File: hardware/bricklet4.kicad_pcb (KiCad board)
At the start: 4 copper layers, 102 x 85 mm, 102 parts, among them J101 TNG-Power-TOP, J102 TNG-Power-BTM, J103 TNG-Data-TOP, J104 TNG-Data-BTM, P102 Debug, P103 PE, P201 CON-SENSOR2, P202 CON-SENSOR2, P203 CON-SENSOR2, P204 CON-SENSOR2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

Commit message: fix slew rate bug, mark C as DNP
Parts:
- C206: value 1uF -> DNP

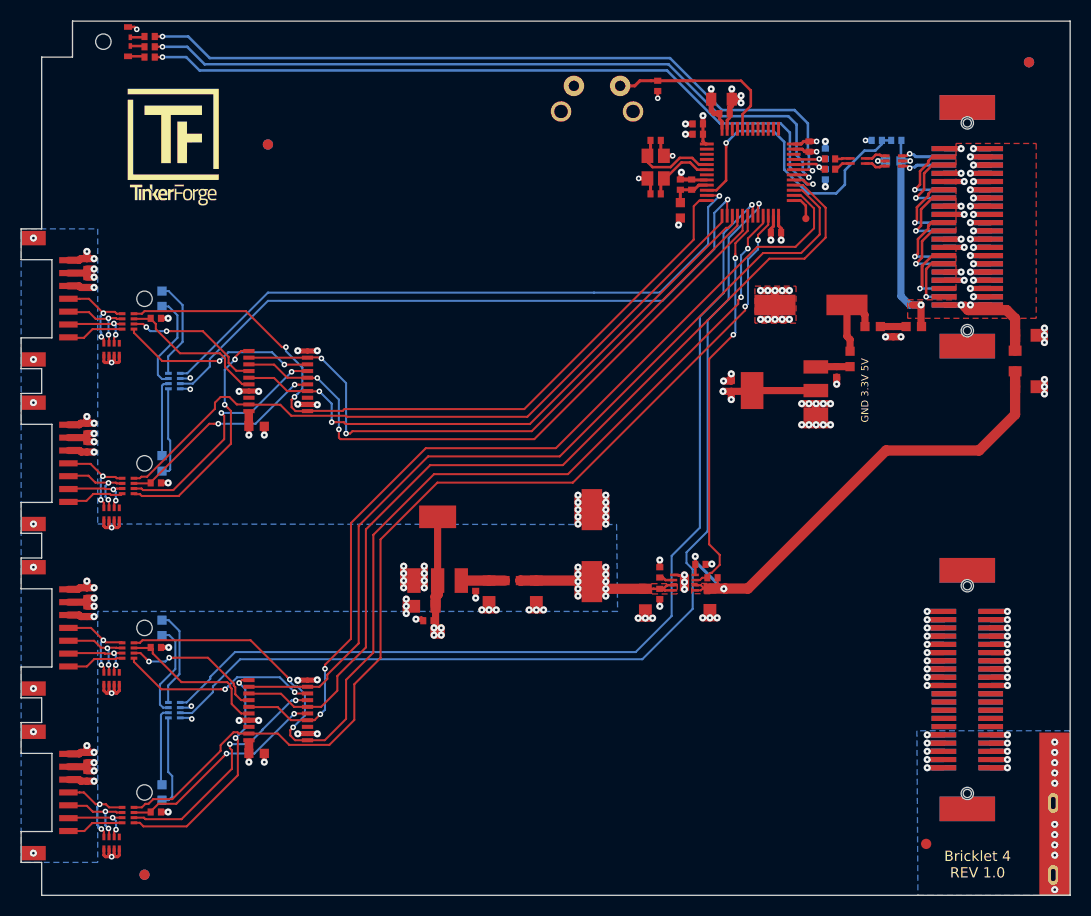
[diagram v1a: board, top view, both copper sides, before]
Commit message: version 1.1
fix footprints
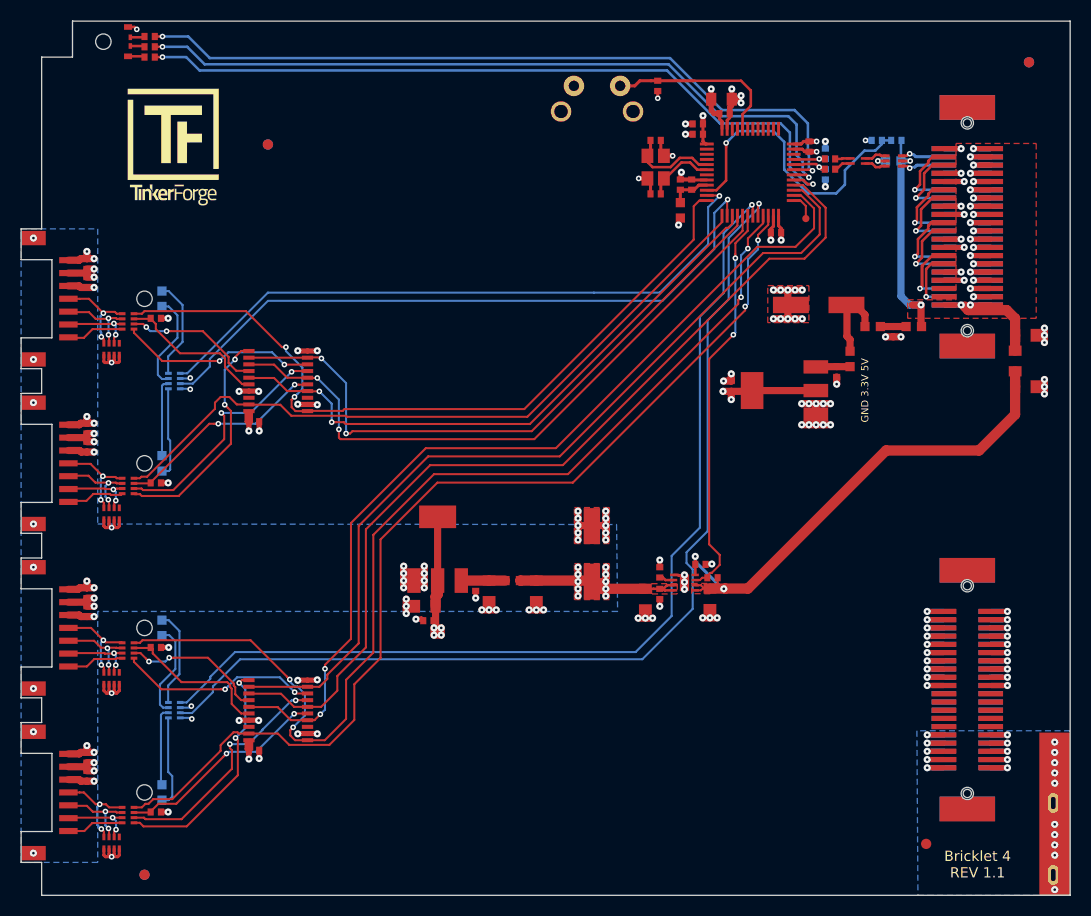
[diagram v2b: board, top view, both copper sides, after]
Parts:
- C111, C209: value TBD -> 100µF; footprint kicad-libraries:ELKO_83 -> kicad-libraries:ELKO_63
- C201, C202: footprint kicad-libraries:C0603F -> kicad-libraries:C0402F
- LED101: footprint kicad-libraries:LED-RGB-LP -> LED-RGB-LP
- moved C209 0.80 mm to (143.3, 114.3)
- moved C111 0.75 mm to (165.3, 90.1)
- moved C201 0.51 mm to (110.5, 101.5)
- moved C202 0.39 mm to (110.5, 133.4)
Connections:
- CP201 pad 1: (no net) -> Net-(CP201-Pad1)
- CP202 pad 1: (no net) -> Net-(CP202-Pad1)
- CP203 pad 1: (no net) -> Net-(CP203-Pad1)
- CP204 pad 1: (no net) -> Net-(CP204-Pad1)
- J101 pad 21: (no net) -> Net-(J101-Pad21)
- J101 pad 22: (no net) -> Net-(J101-Pad22)
- J101 pad 23: (no net) -> Net-(J101-Pad23)
- J101 pad 24: (no net) -> Net-(J101-Pad24)
- J101 pad 25: (no net) -> Net-(J101-Pad25)
- J101 pad 26: (no net) -> Net-(J101-Pad26)
- J101 pad 27: (no net) -> Net-(J101-Pad27)
- J101 pad 28: (no net) -> Net-(J101-Pad28)
- J101 pad 29: (no net) -> Net-(J101-Pad29)
- J101 pad 30: (no net) -> Net-(J101-Pad30)
- J102 pad 21: (no net) -> Net-(J102-Pad21)
- J102 pad 22: (no net) -> Net-(J102-Pad22)
- J102 pad 23: (no net) -> Net-(J102-Pad23)
- J102 pad 24: (no net) -> Net-(J102-Pad24)
- J102 pad 25: (no net) -> Net-(J102-Pad25)
- J102 pad 26: (no net) -> Net-(J102-Pad26)
- J102 pad 27: (no net) -> Net-(J102-Pad27)
- J102 pad 28: (no net) -> Net-(J102-Pad28)
- J102 pad 29: (no net) -> Net-(J102-Pad29)
- J102 pad 30: (no net) -> Net-(J102-Pad30)
- J103 pad 35: (no net) -> Net-(J103-Pad35)
- J103 pad 37: (no net) -> Net-(J103-Pad37)
- U101 pad 2: (no net) -> Net-(U101-Pad2)
- U101 pad 3: (no net) -> Net-(U101-Pad3)
- U101 pad 34: (no net) -> Net-(U101-Pad34)
- U101 pad 37: (no net) -> Net-(U101-Pad37)
- U101 pad 38: (no net) -> Net-(U101-Pad38)
- U101 pad 39: (no net) -> Net-(U101-Pad39)
- U101 pad 4: (no net) -> Net-(U101-Pad4)
- U101 pad 40: (no net) -> LED0
- U101 pad 41: (no net) -> LED1
- U101 pad 42: (no net) -> LED2
- U101 pad 43: (no net) -> LED3
- U101 pad 45: (no net) -> Net-(U101-Pad45)
- U101 pad 46: (no net) -> Net-(U101-Pad46)
- U101 pad 7: (no net) -> Net-(U101-Pad7)
- U201 pad 18: (no net) -> Net-(U201-Pad18)
- U201 pad 3: (no net) -> Net-(U201-Pad3)
- U202 pad 18: (no net) -> Net-(U202-Pad18)
- U202 pad 3: (no net) -> Net-(U202-Pad3)
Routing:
- net B-3V3: track 194.9 -> 195.6 mm
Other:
- board text added: "Bricklet 4 REV 1.1"
- board text added: "Copyright Tinkerforge GmbH 2020. This documentation describes Open Hardware and is licensed under the CERN OHL v. 1.1. You may redistribute and modify this documentation under the terms of the CERN OHL v.1.1. (http://ohwr.org/cernohl). This documentation is distributed WITHOUT ANY EXPRESS OR IMPLIED WARRANTY, INCLUDING OF MERCHANTABILITY, SATISFACTORY QUALITY AND FITNESS FOR A PARTICULAR PURPOSE.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"
- board text removed: "Bricklet 4 REV 1.0"

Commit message: update tbd
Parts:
- C108, C109: value TBD -> 33pF
- X101: value TBD -> 8MHz

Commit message: specify capacitors
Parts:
- C113, C114: value TBD/47pF -> 47pF

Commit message: fix values
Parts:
- C110: footprint C0805 -> kicad-libraries:C0805E
- C203, C204, C207, C210, C211, C222, C223: footprint kicad-libraries:C0805 -> kicad-libraries:C0805E
- moved R205 0.12 mm to (155.0, 116.5)

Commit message: fix values
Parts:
- C111, C209: value 100µF -> 100uF
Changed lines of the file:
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@@
       (effects (font (size 0.59944 0.59944) (thickness 0.12446)))
     )
-    (fp_text value 100µF (at 0.95 -0.375) (layer F.Fab)
+    (fp_text value 100uF (at 0.95 -0.375) (layer F.Fab)
       (effects (font (size 0.59944 0.59944) (thickness 0.12446)))
     )
@@
       (effects (font (size 0.59944 0.59944) (thickness 0.12446)))
     )
-    (fp_text value 100µF (at 0.95 -0.375 90) (layer F.Fab)
+    (fp_text value 100uF (at 0.95 -0.375 90) (layer F.Fab)
       (effects (font (size 0.59944 0.59944) (thickness 0.12446)))
     )

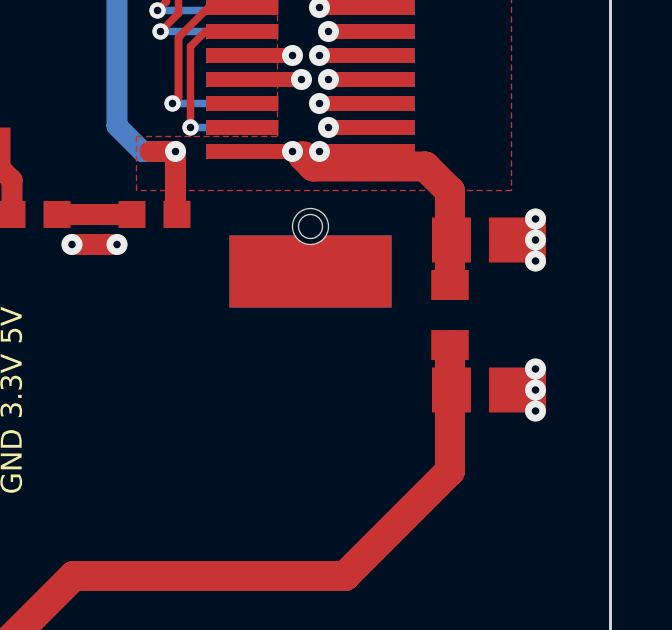
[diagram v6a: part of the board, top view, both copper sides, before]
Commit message: fix footprint
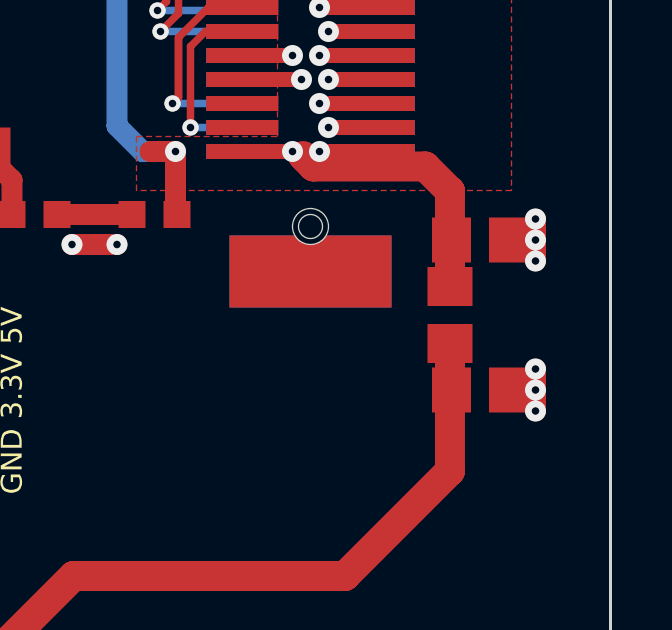
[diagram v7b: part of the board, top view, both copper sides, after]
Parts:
- L201: footprint kicad-libraries:R0805 -> kicad-libraries:R0805E

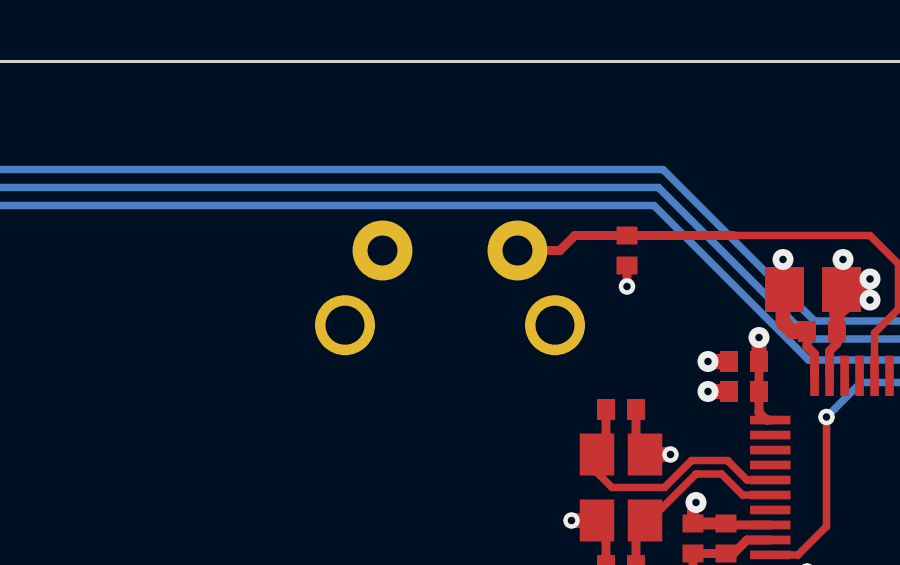
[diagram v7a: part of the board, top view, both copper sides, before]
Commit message: all footprints updated
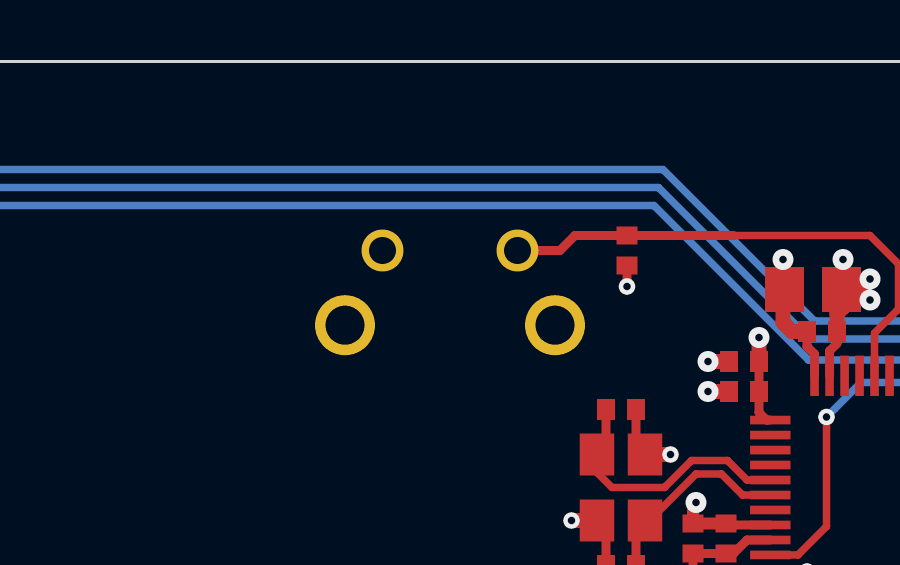
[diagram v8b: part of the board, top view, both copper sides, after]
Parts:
- C101, C102, C103, C104, C105, C106, C107, C108, C109, C112, C113, C114, C116, C117: footprint C0402F -> kicad-libraries:C0402F
- C115: footprint C0603F -> kicad-libraries:C0603F
- J101, J103: footprint TNG-40-TOP -> kicad-libraries:TNG-40-TOP
- J102, J104: footprint TNG-40-BTM -> kicad-libraries:TNG-40-BTM
- L101, L102, L103, L104, L202: footprint R0603F -> kicad-libraries:R0603F
- L105: footprint WE-CNSW-0603 -> kicad-libraries:WE-CNSW-0603
- LED101: footprint LED-RGB-LP -> kicad-libraries:LED-RGB-LP
- R101, R102, R103, R104, R105, R106, R107, R108: footprint R0402F -> kicad-libraries:R0402F
- U103: footprint SOT563-SPEC -> kicad-libraries:SOT563-SPEC
